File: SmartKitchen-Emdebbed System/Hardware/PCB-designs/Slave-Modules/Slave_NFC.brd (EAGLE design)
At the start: 100 x 80 mm, 34 parts, among them IC1 PCF8574T, IC2 7805DT, IC3 PCF8574T, IC4 74AHC1G126DBV, J1 RJ11-2L-B, J2 RJ11-2L-B, Q1 SPB80P06P, Q2 SPB80P06P, Q3 SPB80P06P, X1 22-23-2101

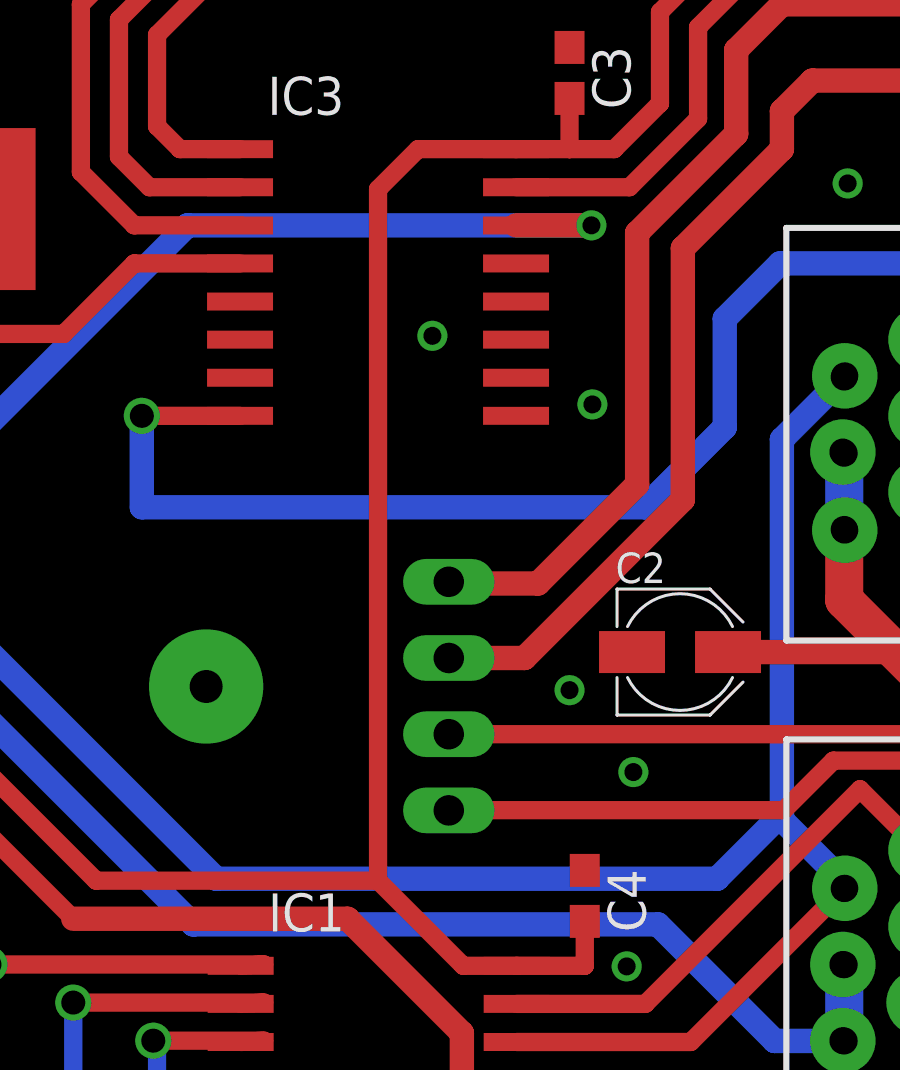
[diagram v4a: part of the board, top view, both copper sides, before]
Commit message: adding pull-ups and inh-capacitors to list
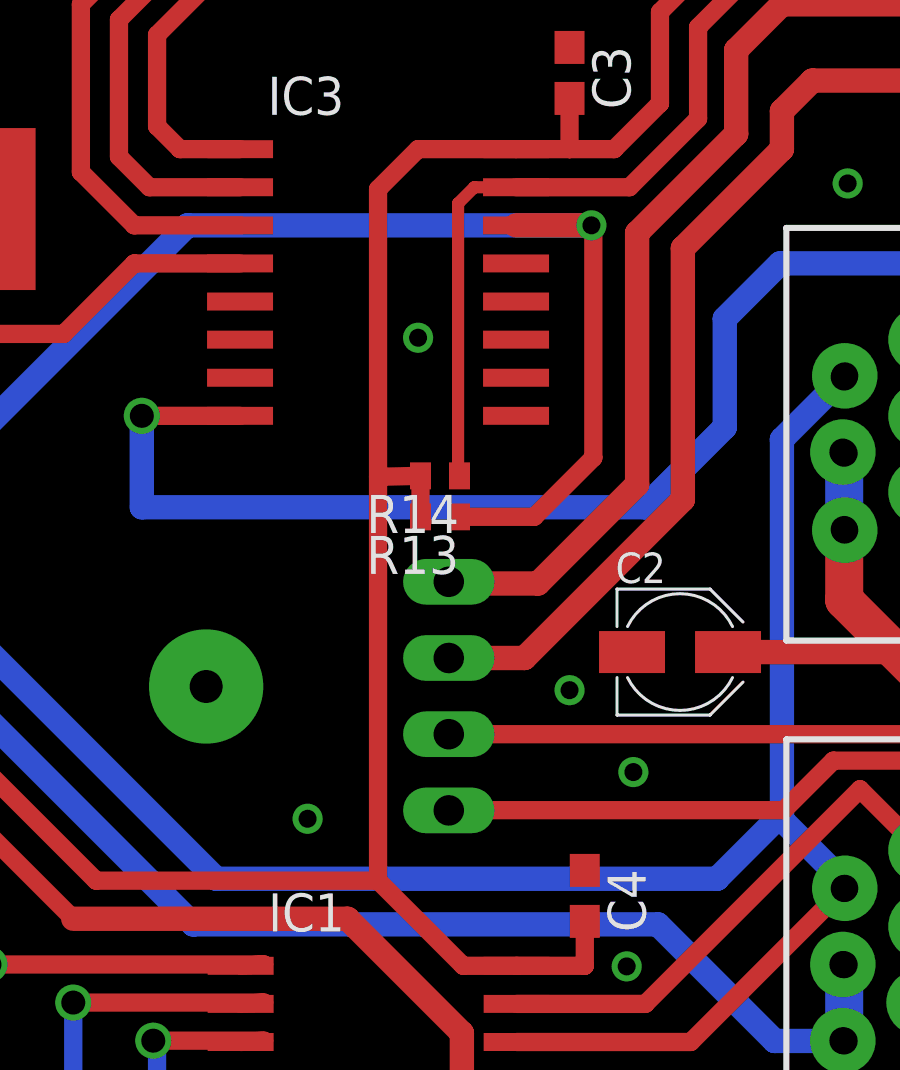
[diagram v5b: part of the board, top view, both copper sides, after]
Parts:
- added R13, R14: 4k7, rcl:R0402
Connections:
- net N$1: now also R14.1
- net N$21: now also R13.2, R14.2
- net N$3: now also R13.1
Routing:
- net N$3: track 96.0 -> 109.1 mm
- net N$1: track 89.3 -> 100.6 mm
- net N$21: track 229.9 -> 232.6 mm
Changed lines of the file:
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@@
 <element name="C3" library="resistor" package="C0603" value="100n" x="75.565" y="60.452" rot="R270"/>
 <element name="C4" library="resistor" package="C0603" value="100n" x="76.073" y="33.02" rot="R270"/>
+<element name="R13" library="rcl" package="R0402" value="4k7" x="71.247" y="45.6565" rot="R180"/>
+<element name="R14" library="rcl" package="R0402" value="4k7" x="71.247" y="47.02175" rot="R180"/>
 </elements>
 <signals>
@@
 <via x="53.34" y="32.893" extent="1-16" drill="0.6" shape="square"/>
 <via x="84.836" y="56.769" extent="1-16" drill="0.6" shape="square"/>
-<via x="76.327" y="49.403" extent="1-16" drill="0.6" shape="square"/>
+<via x="66.83375" y="35.59175" extent="1-16" drill="0.6" shape="square"/>
 <via x="10.541" y="68.707" extent="1-16" drill="0.6" shape="square"/>
 <via x="15.24" y="76.962" extent="1-16" drill="0.6" shape="square"/>
@@
 <via x="10.541" y="17.907" extent="1-16" drill="0.6" shape="square"/>
 <via x="84.709" y="16.256" extent="1-16" drill="0.6" shape="square"/>
-<via x="70.993" y="51.689" extent="1-16" drill="0.6" shape="square"/>
+<via x="70.51675" y="51.6255" extent="1-16" drill="0.6" shape="square"/>
 <via x="4.064" y="56.134" extent="1-16" drill="0.6" shape="square"/>
 <via x="8.001" y="51.308" extent="1-16" drill="0.6" shape="square"/>
@@
 <wire x1="85.2475" y1="36.576" x2="78.0915" y2="29.42" width="0.6096" layer="1"/>
 <wire x1="78.0915" y1="29.42" x2="73.8025" y2="29.42" width="0.6096" layer="1"/>
+<contactref element="R14" pad="1"/>
+<wire x1="71.897" y1="47.02175" x2="71.85025" y2="47.02175" width="0.4064" layer="1"/>
+<wire x1="71.85025" y1="47.02175" x2="71.85025" y2="56.10225" width="0.4064" layer="1"/>
+<wire x1="71.85025" y1="56.10225" x2="72.39" y2="56.642" width="0.4064" layer="1"/>
+<wire x1="72.39" y1="56.642" x2="73.782" y2="56.642" width="0.4064" layer="1"/>
 </signal>
 <signal name="N$12">
@@
 <via x="76.294" y="55.372" extent="1-16" drill="0.6" shape="square"/>
 <wire x1="76.294" y1="55.372" x2="73.782" y2="55.372" width="0.8128" layer="1"/>
+<contactref element="R13" pad="1"/>
+<wire x1="71.897" y1="45.6565" x2="74.39025" y2="45.6565" width="0.6096" layer="1"/>
+<wire x1="74.39025" y1="45.6565" x2="76.35875" y2="47.625" width="0.6096" layer="1"/>
+<wire x1="76.35875" y1="47.625" x2="76.35875" y2="55.30725" width="0.6096" layer="1"/>
+<wire x1="76.35875" y1="55.30725" x2="76.294" y2="55.372" width="0.6096" layer="1"/>
 </signal>
 <signal name="N$21">
@@
 <wire x1="73.782" y1="57.912" x2="70.5155" y2="57.912" width="0.6096" layer="1"/>
 <wire x1="70.5155" y1="57.912" x2="69.182" y2="56.5785" width="0.6096" layer="1"/>
-<wire x1="69.182" y1="56.5785" x2="69.182" y2="33.528" width="0.6096" layer="1"/>
+<wire x1="69.182" y1="56.5785" x2="69.182" y2="46.99" width="0.6096" layer="1"/>
 <contactref element="C4" pad="2"/>
 <contactref element="C3" pad="2"/>
+<wire x1="69.182" y1="46.99" x2="69.182" y2="33.528" width="0.6096" layer="1"/>
 <wire x1="73.8025" y1="30.69" x2="76.073" y2="30.69" width="0.6096" layer="1"/>
 <wire x1="76.073" y1="30.69" x2="76.073" y2="32.17" width="0.6096" layer="1"/>
 <wire x1="75.565" y1="59.602" x2="75.565" y2="57.912" width="0.6096" layer="1"/>
+<contactref element="R13" pad="2"/>
+<contactref element="R14" pad="2"/>
+<wire x1="70.597" y1="47.02175" x2="69.182" y2="46.99" width="0.6096" layer="1"/>
+<wire x1="70.597" y1="45.6565" x2="70.597" y2="47.02175" width="0.6096" layer="1"/>
 <wire x1="51.2115" y1="46.2005" x2="51.209" y2="46.198" width="0" layer="19" extent="1-1"/>
 </signal>
